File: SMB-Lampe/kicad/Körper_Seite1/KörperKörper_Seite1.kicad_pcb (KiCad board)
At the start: 2 copper layers, 123 x 95.7 mm, 24 parts, among them J1 Conn_01x01_Pin, J2 Conn_01x01_Pin, J3 Conn_01x01_Pin, J4 Conn_01x01_Pin, J5 Conn_01x01_Pin, J6 Conn_01x01_Pin

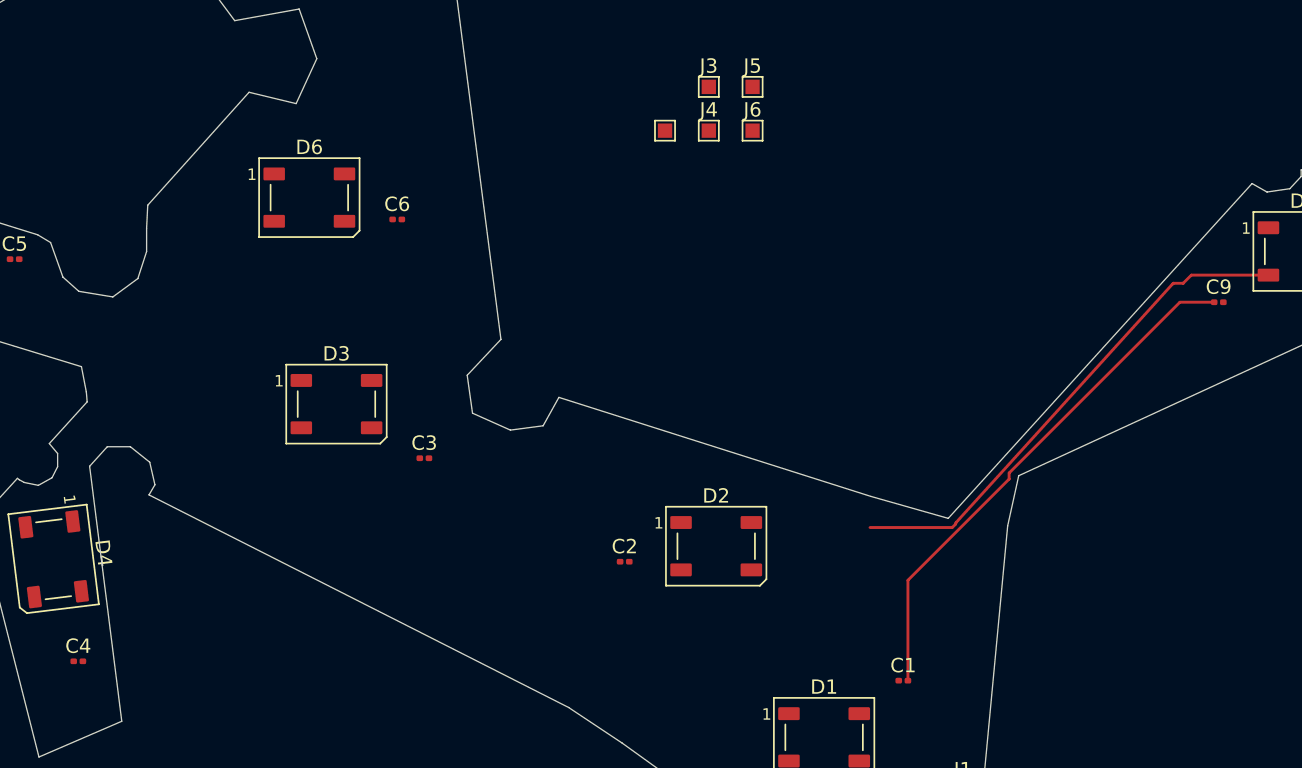
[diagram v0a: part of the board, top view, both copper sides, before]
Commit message: Alle Platinen erstellt
Alle Platinen wurden im Projekt einzeln erstellt.
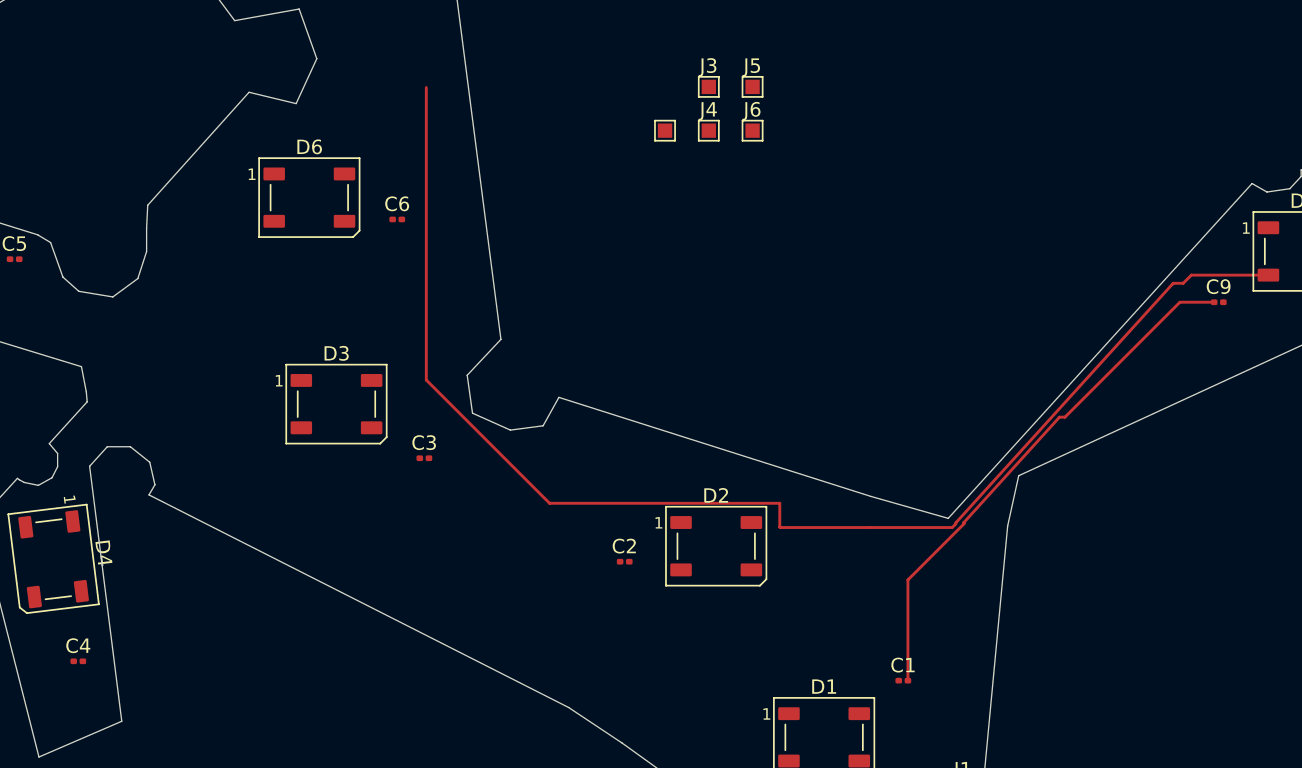
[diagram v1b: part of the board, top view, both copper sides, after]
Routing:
- net Net-(D8-DIN): track 35.6 -> 92.1 mm
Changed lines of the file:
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@@
 		(tags "LED RGB NeoPixel PLCC-4 5050")
 		(property "Reference" "D4"
-			(at 0 -3.5 97)
+			(at 0 -3.500001 97)
 			(layer "F.SilkS")
 			(effects
@@
 	)
 	(segment
-		(start 191.351803 90.52)
-		(end 179.453758 102.418045)
+		(start 182.962015 98.528125)
+		(end 183.343678 98.528125)
 		(width 0.2)
 		(layer "F.Cu")
@@
 	)
 	(segment
-		(start 179.453758 102.841225)
-		(end 172.4 109.894983)
+		(start 176.30648 105.964395)
+		(end 176.30648 105.862734)
 		(width 0.2)
 		(layer "F.Cu")
@@
 	)
 	(segment
-		(start 179.453758 102.418045)
-		(end 179.453758 102.841225)
+		(start 172.4 109.870875)
+		(end 176.30648 105.964395)
 		(width 0.2)
 		(layer "F.Cu")
@@
 	)
 	(segment
-		(start 193.74 90.52)
+		(start 183.343678 98.528125)
 		(end 191.351803 90.52)
 		(width 0.2)
@@
 	)
 	(segment
-		(start 172.4 109.894983)
-		(end 172.4 116.89)
+		(start 191.351803 90.52)
+		(end 193.74 90.52)
+		(width 0.2)
+		(layer "F.Cu")
+		(net 1)
+	)
+	(segment
+		(start 172.4 116.89)
+		(end 172.4 109.870875)
+		(width 0.2)
+		(layer "F.Cu")
+		(net 1)
+	)
+	(segment
+		(start 176.30648 105.862734)
+		(end 176.309408 105.859806)
+		(width 0.2)
+		(layer "F.Cu")
+		(net 1)
+	)
+	(segment
+		(start 176.309408 105.859806)
+		(end 176.309408 105.859507)
 		(width 0.2)
 		(layer "F.Cu")
@@
 	)
 	(segment
+		(start 176.309408 105.859507)
+		(end 182.962015 98.528125)
+		(width 0.2)
+		(layer "F.Cu")
+		(net 1)
+	)
+	(segment
+		(start 163.47 106.194548)
+		(end 163.47 104.53)
+		(width 0.2)
+		(layer "F.Cu")
+		(net 11)
+	)
+	(segment
 		(start 190.821495 89.27)
 		(end 175.749704 105.879585)
@@
 	)
 	(segment
+		(start 163.47 104.53)
+		(end 147.43 104.53)
+		(width 0.2)
+		(layer "F.Cu")
+		(net 11)
+	)
+	(segment
 		(start 192.15 88.63)
 		(end 191.58 89.2)
@@
 	)
 	(segment
+		(start 138.84 95.94)
+		(end 138.84 75.56)
+		(width 0.2)
+		(layer "F.Cu")
+		(net 11)
+	)
+	(segment
+		(start 169.76 106.22)
+		(end 163.495452 106.22)
+		(width 0.2)
+		(layer "F.Cu")
+		(net 11)
+	)
+	(segment
+		(start 147.43 104.53)
+		(end 138.84 95.94)
+		(width 0.2)
+		(layer "F.Cu")
+		(net 11)
+	)
+	(segment
 		(start 175.720179 105.983596)
 		(end 175.483775 106.22)
@@
 		(width 0.2)
 		(layer "F.Cu")
+		(net 11)
+	)
+	(segment
+		(start 163.495452 106.22)
+		(end 163.47 106.194548)
+		(width 0.2)
+		(layer "F.Cu")
